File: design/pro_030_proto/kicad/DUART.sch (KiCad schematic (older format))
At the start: 27 parts, among them IC8 XR68C681CJTR-F-XR68C681, J1 Conn_01x06_Male, J2 Conn_01x06_Male, J3 Conn_02x08_Odd_Even, Y1 3.6864MHz

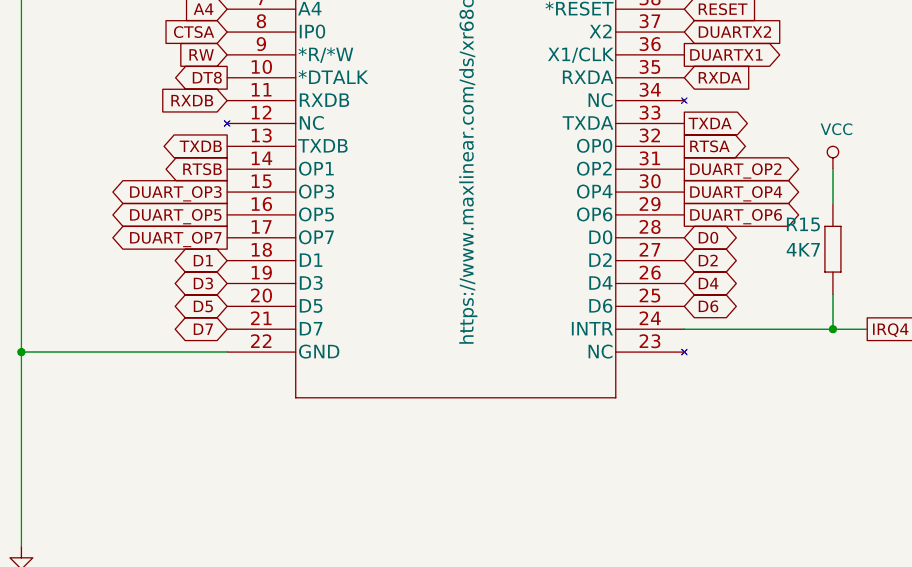
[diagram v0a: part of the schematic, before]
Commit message: Fix (another) hilarious mistake 😞
* 8-bit ports wired to the wrong end of the bus
* Another respin needed I think...
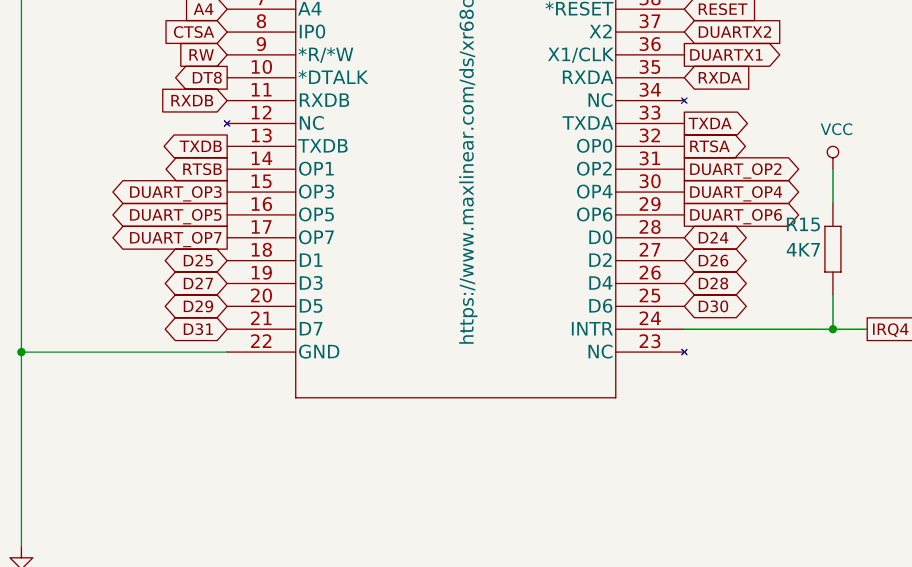
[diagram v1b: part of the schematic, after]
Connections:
- net D0 renamed D24
- net D1 renamed D25
- net D2 renamed D26
- net D3 renamed D27
- net D4 renamed D28
- net D5 renamed D29
- net D6 renamed D30
- net D7 renamed D31
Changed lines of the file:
@@
 RW
 Text GLabel 4000 3450 2    50   BiDi ~ 0
-D0
+D24
 Text GLabel 4000 3550 2    50   BiDi ~ 0
-D2
+D26
 Text GLabel 4000 3650 2    50   BiDi ~ 0
-D4
+D28
 Text GLabel 4000 3750 2    50   BiDi ~ 0
-D6
+D30
 Text GLabel 2000 3550 0    50   BiDi ~ 0
-D1
+D25
 Text GLabel 2000 3650 0    50   BiDi ~ 0
-D3
+D27
 Text GLabel 2000 3750 0    50   BiDi ~ 0
-D5
+D29
 Text GLabel 2000 3850 0    50   BiDi ~ 0
-D7
+D31
 Text GLabel 4000 3050 2    50   Output ~ 0
 RTSA

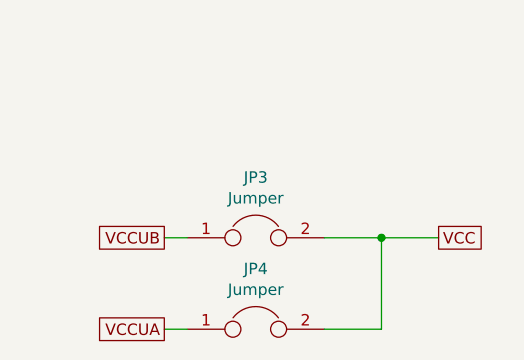
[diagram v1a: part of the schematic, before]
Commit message: Add legacy SD / SPI header
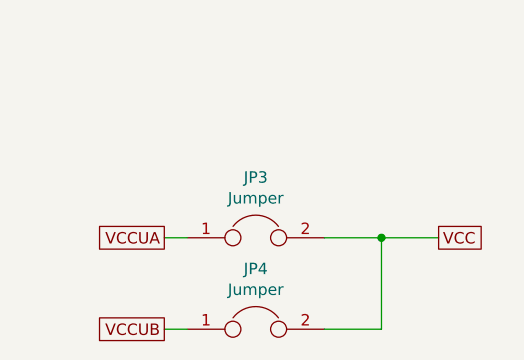
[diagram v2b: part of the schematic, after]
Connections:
- net VCCUA: now also JP3.1; no longer JP4.1
- net VCCUB: now also JP4.1; no longer JP3.1
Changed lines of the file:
@@
 Text GLabel 6800 5600 2    50   Input ~ 0
 P_RTSB
+Text GLabel 1650 7050 0    50   UnSpc ~ 0
+VCCUB
 Text GLabel 1650 6650 0    50   UnSpc ~ 0
-VCCUB
-Text GLabel 1650 7050 0    50   UnSpc ~ 0
 VCCUA
 $Comp
